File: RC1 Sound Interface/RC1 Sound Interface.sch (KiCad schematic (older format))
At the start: 35 parts, among them J1 Expansion, J2 ADDRESS, U1 SID, U2 SID

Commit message: Sound Interface layout done
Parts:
- C11, C12, C13, C14, C17, C18, C19: renamed from C?; footprint (none) -> Capacitors_THT:CP_Radial_D5.0mm_P2.50mm
- J2: footprint Pin_Headers:Pin_Header_Straight_2x09_Pitch2.54mm -> Pin_Headers:Pin_Header_Straight_2x06_Pitch2.54mm
- J3: renamed from J?; footprint (none) -> Pin_Headers:Pin_Header_Straight_2x05_Pitch2.54mm
- J4: renamed from J?; footprint (none) -> TRS:Tayda_3.5mm_stereo_TRS_jack_A-853
- R1, R2, R3, R4: renamed from R?; footprint (none) -> Resistors_THT:R_Axial_DIN0207_L6.3mm_D2.5mm_P10.16mm_Horizontal
- RV1, RV2: renamed from RV?; footprint (none) -> Potentiometer:Potentiometer_Trimmer_Bourns_3296W
- U1: value SID -> SID #1; footprint (none) -> Housings_DIP:DIP-28_W15.24mm_Socket
- U2, U4: renamed from U?; footprint (none) -> Housings_DIP:DIP-8_W7.62mm_Socket
- U3: renamed from U2; value SID -> SID #2; footprint (none) -> Housings_DIP:DIP-28_W15.24mm_Socket
- gave numbers to parts that had none: 10
- renumbered C2 to C3, C3 to C5, C4 to C6
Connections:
- net A12: now also U5.6 (E3); no longer U6.6 (E3)
- net PHI2: no longer U5.6 (E3)
- net VCC: now also U6.6 (E3)
- net ~SID1: no longer U3.8 (~CS)
- net ~SID2: now also U3.8 (~CS)
- net at C17.1, U2.5: now also C15.2; no longer C15.1
- net at R1.1: now also C15.1; no longer C15.2
- net at C18.1, U4.5: now also C16.2; no longer C16.1
- net at R2.1: now also C16.1; no longer C16.2
- net A5: no longer names the net of J1.11 (A5)
- net A6: no longer names the net of J1.10 (A6)
- net A7: no longer names the net of J1.9 (A7)
- net A8: no longer names the net of J1.8 (A8)
- no-connect marks 25 -> 29

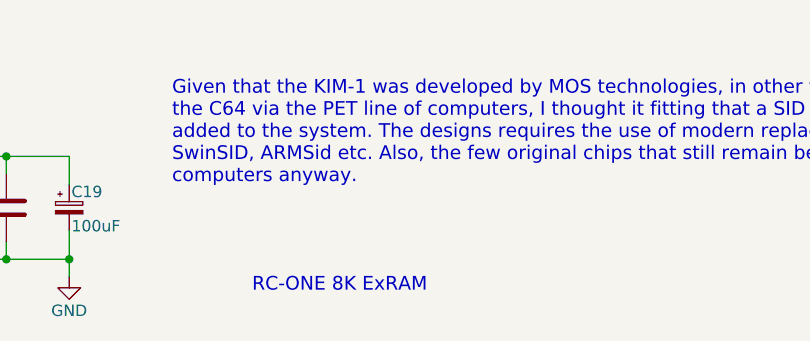
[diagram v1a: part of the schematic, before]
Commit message: Wrong schematic name
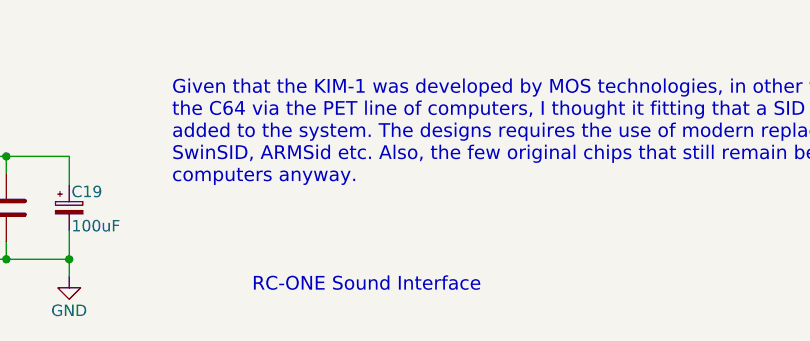
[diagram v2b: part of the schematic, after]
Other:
- note added: "RC-ONE Sound Interface"
- note removed: "RC-ONE 8K ExRAM"
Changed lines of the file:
@@
 $EndComp
 Text Notes 12175 10925 0    60   ~ 0
-RC-ONE 8K ExRAM
+RC-ONE Sound Interface
 NoConn ~ 14750 5275
 NoConn ~ 14750 7075

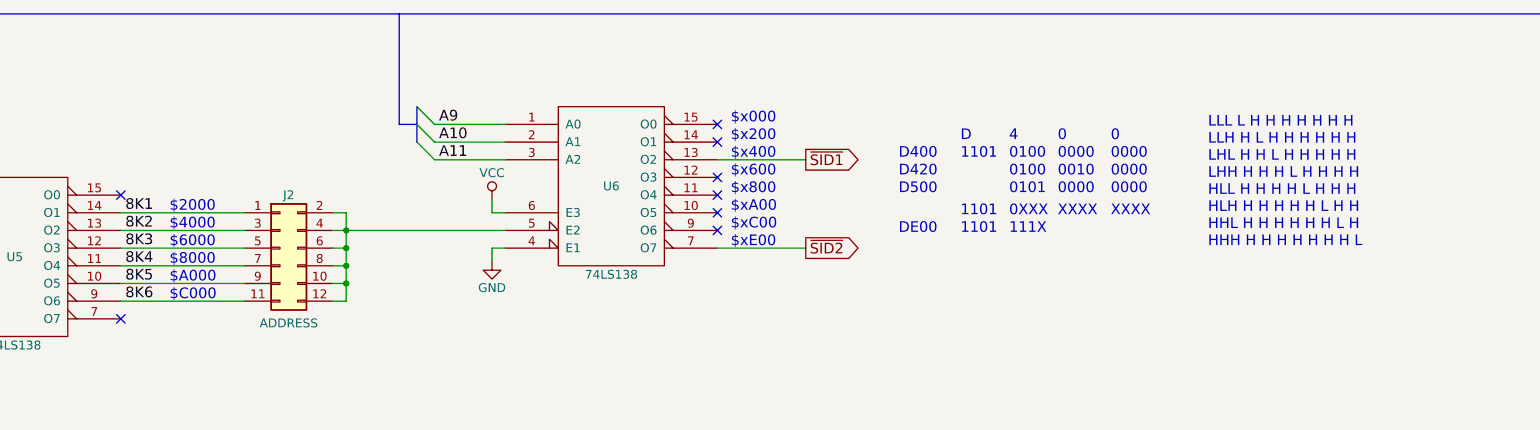
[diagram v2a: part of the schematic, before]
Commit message: Address calculations fixed
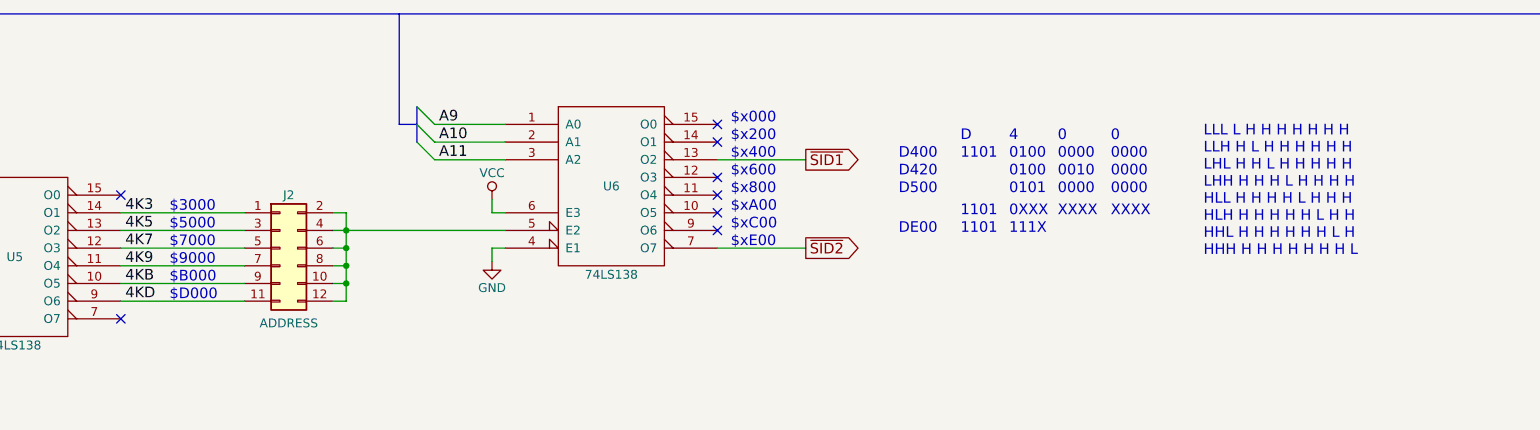
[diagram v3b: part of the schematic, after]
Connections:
- net 8K1 renamed 4K3
- net 8K2 renamed 4K5
- net 8K3 renamed 4K7
- net 8K4 renamed 4K9
- net 8K5 renamed 4KB
- net 8K6 renamed 4KD
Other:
- note added: "$3000"
- note added: "$5000"
- note added: "$7000"
- note added: "$9000"
- note added: "$B000"
- note added: "$D000"
- note removed: "$2000"
- note removed: "$4000"
- note removed: "$6000"
- note removed: "$8000"
- note removed: "$A000"
- note removed: "$C000"
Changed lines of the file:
@@
 Title ""
 Date ""
-Rev ""
+Rev "B"
 Comp ""
 Comment1 ""
@@
 $EndComp
 Text Label 2550 2400 0    60   ~ 0
-8K1
+4K3
 Text Label 2550 2500 0    60   ~ 0
-8K2
+4K5
 Text Label 2550 2600 0    60   ~ 0
-8K3
+4K7
 Entry Wire Line
 	825  2200 925  2300
@@
 	825  2400 925  2500
 Text Notes 2800 2400 0    60   ~ 0
-$2000
+$3000
 Text Notes 2800 2500 0    60   ~ 0
-$4000
+$5000
 Text Notes 2800 2600 0    60   ~ 0
-$6000
+$7000
 Text Notes 2800 2700 0    60   ~ 0
-$8000
+$9000
 Text Notes 2800 2800 0    60   ~ 0
-$A000
+$B000
 Text Notes 2800 2900 0    60   ~ 0
-$C000
+$D000
 $Comp
 L C C6
@@
 	14250 7075 14350 7175
 Text Label 2550 2700 0    60   ~ 0
-8K4
+4K9
 Text Label 2550 2800 0    60   ~ 0
-8K5
+4KB
 Text Label 2550 2900 0    60   ~ 0
-8K6
+4KD
 NoConn ~ 14750 5675
 NoConn ~ 14750 5375
@@
 Text Notes 8125 2000 0    60   ~ 0
 0
-Text Notes 8675 2600 0    60   ~ 0
+Text Notes 8650 2650 0    60   ~ 0
 LLL L H H H H H H H\nLLH H L H H H H H H\nLHL H H L H H H H H\nLHH H H H L H H H H\nHLL H H H H L H H H\nHLH H H H H H L H H\nHHL H H H H H H L H\nHHH H H H H H H H L
 Text Notes 7550 2425 0    60   ~ 0
